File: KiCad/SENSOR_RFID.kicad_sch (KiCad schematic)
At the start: 0 parts

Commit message: Diagrama blocs versió 4 + BOM actualitzat + Bus CAN i USART + Lector RFID
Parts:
- added J2: Conn_01x08_Pin, symbol Connector:Conn_01x08_Pin
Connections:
- new net GND_POWER: J2.6 (GND)
- new net MISO: J2.4 (MISO)
- new net MOSI: J2.3 (MOSI)
- new net RST: J2.5 (IRQ)
- new net SCK: J2.2 (SCK)
- new net SDA (SS): J2.1 (SDA)
- new net VDD_3V3: J2.8 (3.3V)
- no-connect marks 0 -> 1
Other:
- note added: "master in"
- note added: "master out"
- note added: "reset"
- note added: "serial clock"
- note added: "slave select"

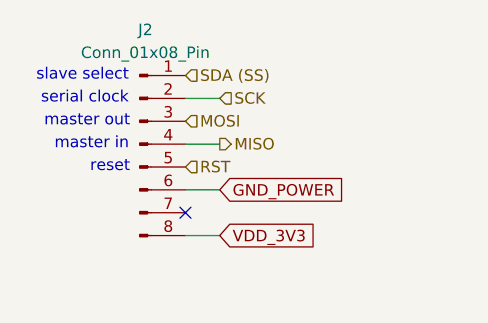
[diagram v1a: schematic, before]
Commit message: Footprints afegides a Comunicació, Sensor RFID i Sensor Corrent
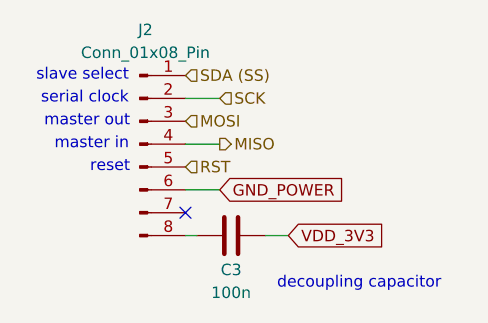
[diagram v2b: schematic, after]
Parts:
- added C3: 100n, symbol Device:C
- J2: footprint (none) -> Connector_PinSocket_1.00mm:PinSocket_1x08_P1.00mm_Vertical
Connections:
- net VDD_3V3: now also C3.2; no longer J2.8 (3.3V)
- new net: C3.1, J2.8 (3.3V)
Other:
- note added: "decoupling capacitor"
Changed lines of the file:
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@@
 	(generator_version "9.0")
 	(paper "A4")
+	(text "decoupling capacitor"
+		(exclude_from_sim no)
+		(at 171.704 81.534 0)
+		(effects
+			(font
+				(size 1.27 1.27)
+			)
+		)
+	)
 	(text "slave select"
 		(exclude_from_sim no)
@@
 	(wire
 		(pts
-			(xy 152.4 76.2) (xy 156.21 76.2)
+			(xy 152.4 76.2) (xy 153.67 76.2)
 		)
 		(stroke
@@
 		(pts
 			(xy 152.4 60.96) (xy 156.21 60.96)
+		)
+		(stroke
+			(width 0)
+			(type default)
+		)
+	)
+	(wire
+		(pts
+			(xy 161.29 76.2) (xy 163.83 76.2)
 		)
 		(stroke
@@
 	(global_label "VDD_3V3"
 		(shape input)
-		(at 156.21 76.2 0)
+		(at 163.83 76.2 0)
 		(fields_autoplaced yes)
 		(effects
@@
 		)
 		(property "Intersheetrefs" "${INTERSHEET_REFS}"
-			(at 167.299 76.2 0)
+			(at 174.919 76.2 0)
 			(effects
 				(font
@@
 			)
 			(justify left)
+		)
+	)
+	(symbol
+		(lib_id "Device:C")
+		(at 157.48 76.2 90)
+		(unit 1)
+		(exclude_from_sim no)
+		(in_bom yes)
+		(on_board yes)
+		(dnp no)
+		(property "Reference" "C3"
+			(at 157.48 80.01 90)
+			(effects
+				(font
+					(size 1.27 1.27)
+				)
+			)
+		)
+		(property "Value" "100n"
+			(at 157.48 82.55 90)
+			(effects
+				(font
+					(size 1.27 1.27)
+				)
+			)
+		)
+		(property "Footprint" ""
+			(at 161.29 75.2348 0)
+			(effects
+				(font
+					(size 1.27 1.27)
+				)
+				(hide yes)
+			)
+		)
+		(property "Datasheet" "~"
+			(at 157.48 76.2 0)
+			(effects
+				(font
+					(size 1.27 1.27)
+				)
+				(hide yes)
+			)
+		)
+		(property "Description" "Unpolarized capacitor"
+			(at 157.48 76.2 0)
+			(effects
+				(font
+					(size 1.27 1.27)
+				)
+				(hide yes)
+			)
+		)
+		(pin "1"
+		)
+		(pin "2"
+		)
+		(instances
+			(project ""
+				(path "/347831db-5db9-4aff-ad32-e56fd770e219/31dcd71e-4130-43cb-a335-13c9e1a3d043"
+					(reference "C3")
+					(unit 1)
+				)
+			)
 		)
 	)
@@
 			)
 		)
-		(property "Footprint" ""
+		(property "Footprint" "Connector_PinSocket_1.00mm:PinSocket_1x08_P1.00mm_Vertical"
 			(at 147.32 66.04 0)
 			(effects

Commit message: H
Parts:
- C3: footprint (none) -> Capacitor_SMD:C_0805_2012Metric_Pad1.18x1.45mm_HandSolder
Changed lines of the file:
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@@
 			)
 		)
-		(property "Footprint" ""
+		(property "Footprint" "Capacitor_SMD:C_0805_2012Metric_Pad1.18x1.45mm_HandSolder"
 			(at 161.29 75.2348 0)
 			(effects
